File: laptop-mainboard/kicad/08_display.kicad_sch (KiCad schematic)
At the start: 8 parts, among them U36 TPD12S016, U37 SY6280_VLCD, U38 MP3389_Backlight

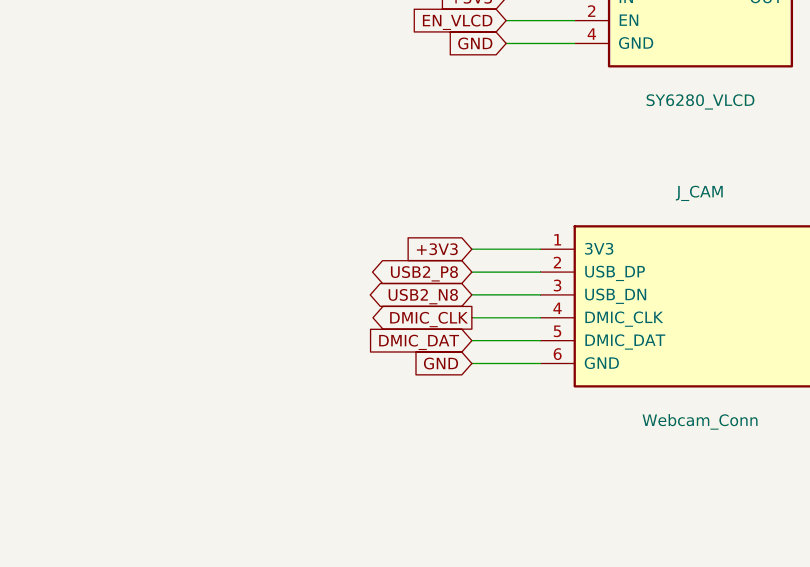
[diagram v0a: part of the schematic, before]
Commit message: Rev B: echte AM5-Pinbelegung, Kleinteile, EliteBook-850-G7-Format
- AM5-Pinmap (1718 Pins, WikiChip/Wikimedia Public Domain) als CSV,
  Sockel-Footprint mit echten Padnamen und 1708 Signal-Netzen im Board
- Blatt 10: MLCC-Baenke, 11 ESD-Arrays, USB2-Chokes, Straps; 48-MHz-Quarz;
  beidseitige Bestueckung (B.Cu) mit Kollisionspruefung pro Seite
- Board 340x112mm im EliteBook-850-G7-Layout: USB-C-100W-PD an der
  Barrel-Jack-Position, TB4/HDMI/USB-A/RJ45 rechts, USB-A/Klinke links,
  HP-Akku 3S/56Wh, HP-FPC-Steckplaetze (Pinouts zu verifizieren)
- GND-Stitching-Vias, MDI-/DP-Korridore, 645 Board-Netze
- Renderer tools/render_board.py erzeugt docs/board_render.png
- Doku: elitebook.md neu, grenzen.md/README/power/layout aktualisiert

Co-Authored-By: Claude Fable 5 <noreply@anthropic.com>
Claude-Session: https://claude.ai/code/session_01E8mU1RUAv938Hs69waADCc
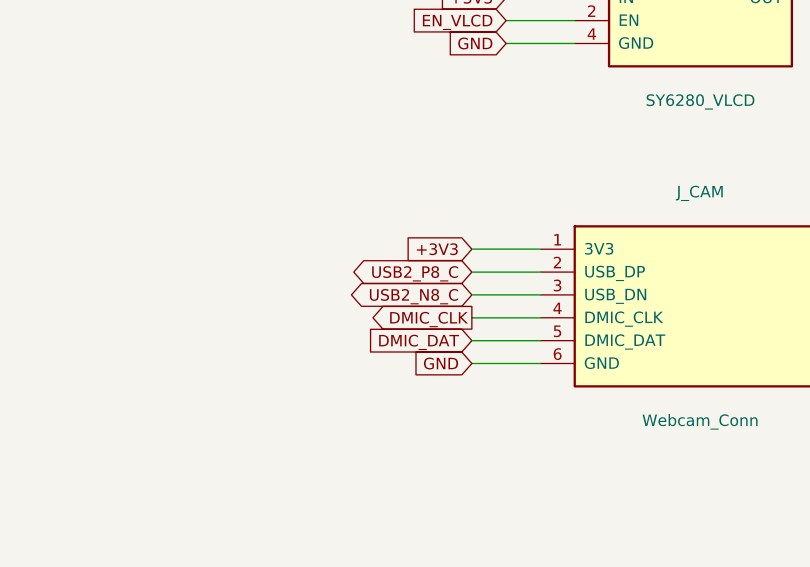
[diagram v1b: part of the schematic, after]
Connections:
- net USB2_N8 renamed USB2_N8_C
- net USB2_P8 renamed USB2_P8_C
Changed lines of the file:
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@@
     (pin "14")
     (pin "15")
-    (instances (project "laptop-mainboard" (path "/d22f2c28-8e23-5b8e-ba77-63ae2c13187c/9dd0bb70-e6d8-5534-8160-b27602d0556d" (reference "J_HDMI") (unit 1))))
+    (instances (project "laptop-mainboard" (path "/d22f2c28-8e23-5b8e-ba77-63ae2c13187c/bf71d2a7-0fa1-5bd7-a7a0-bc950c125fe0" (reference "J_HDMI") (unit 1))))
   )
   (wire (pts (xy 92.22 46.99) (xy 84.6 46.99)) (stroke (width 0) (type default)))
@@
     (pin "12")
     (pin "13")
-    (instances (project "laptop-mainboard" (path "/d22f2c28-8e23-5b8e-ba77-63ae2c13187c/9dd0bb70-e6d8-5534-8160-b27602d0556d" (reference "U36") (unit 1))))
+    (instances (project "laptop-mainboard" (path "/d22f2c28-8e23-5b8e-ba77-63ae2c13187c/bf71d2a7-0fa1-5bd7-a7a0-bc950c125fe0" (reference "U36") (unit 1))))
   )
   (wire (pts (xy 90.95 105.41) (xy 83.33 105.41)) (stroke (width 0) (type default)))
@@
     (pin "11")
     (pin "12")
-    (instances (project "laptop-mainboard" (path "/d22f2c28-8e23-5b8e-ba77-63ae2c13187c/9dd0bb70-e6d8-5534-8160-b27602d0556d" (reference "J_EDP") (unit 1))))
+    (instances (project "laptop-mainboard" (path "/d22f2c28-8e23-5b8e-ba77-63ae2c13187c/bf71d2a7-0fa1-5bd7-a7a0-bc950c125fe0" (reference "J_EDP") (unit 1))))
   )
   (wire (pts (xy 260.95 46.99) (xy 253.33 46.99)) (stroke (width 0) (type default)))
@@
     (pin "3")
     (pin "4")
-    (instances (project "laptop-mainboard" (path "/d22f2c28-8e23-5b8e-ba77-63ae2c13187c/9dd0bb70-e6d8-5534-8160-b27602d0556d" (reference "U37") (unit 1))))
+    (instances (project "laptop-mainboard" (path "/d22f2c28-8e23-5b8e-ba77-63ae2c13187c/bf71d2a7-0fa1-5bd7-a7a0-bc950c125fe0" (reference "U37") (unit 1))))
   )
   (wire (pts (xy 266.03 97.79) (xy 258.41 97.79)) (stroke (width 0) (type default)))
@@
     (pin "5")
     (pin "6")
-    (instances (project "laptop-mainboard" (path "/d22f2c28-8e23-5b8e-ba77-63ae2c13187c/9dd0bb70-e6d8-5534-8160-b27602d0556d" (reference "J_CAM") (unit 1))))
+    (instances (project "laptop-mainboard" (path "/d22f2c28-8e23-5b8e-ba77-63ae2c13187c/bf71d2a7-0fa1-5bd7-a7a0-bc950c125fe0" (reference "J_CAM") (unit 1))))
   )
   (wire (pts (xy 262.22 125.73) (xy 254.6 125.73)) (stroke (width 0) (type default)))
@@
   )
   (wire (pts (xy 262.22 128.27) (xy 254.6 128.27)) (stroke (width 0) (type default)))
-  (global_label "USB2_P8" (shape bidirectional) (at 254.6 128.27 180) (fields_autoplaced yes)
+  (global_label "USB2_P8_C" (shape bidirectional) (at 254.6 128.27 180) (fields_autoplaced yes)
     (effects (font (size 1.27 1.27)) (justify right))
     (property "Intersheetrefs" "${INTERSHEET_REFS}" (at 254.6 128.27 0) (effects (font (size 1.27 1.27)) (hide yes)))
   )
   (wire (pts (xy 262.22 130.81) (xy 254.6 130.81)) (stroke (width 0) (type default)))
-  (global_label "USB2_N8" (shape bidirectional) (at 254.6 130.81 180) (fields_autoplaced yes)
+  (global_label "USB2_N8_C" (shape bidirectional) (at 254.6 130.81 180) (fields_autoplaced yes)
     (effects (font (size 1.27 1.27)) (justify right))
     (property "Intersheetrefs" "${INTERSHEET_REFS}" (at 254.6 130.81 0) (effects (font (size 1.27 1.27)) (hide yes)))
@@
     (pin "6")
     (pin "7")
-    (instances (project "laptop-mainboard" (path "/d22f2c28-8e23-5b8e-ba77-63ae2c13187c/9dd0bb70-e6d8-5534-8160-b27602d0556d" (reference "U38") (unit 1))))
+    (instances (project "laptop-mainboard" (path "/d22f2c28-8e23-5b8e-ba77-63ae2c13187c/bf71d2a7-0fa1-5bd7-a7a0-bc950c125fe0" (reference "U38") (unit 1))))
   )
   (wire (pts (xy 443.49 46.99) (xy 435.87 46.99)) (stroke (width 0) (type default)))
@@
     (pin "1")
     (pin "2")
-    (instances (project "laptop-mainboard" (path "/d22f2c28-8e23-5b8e-ba77-63ae2c13187c/9dd0bb70-e6d8-5534-8160-b27602d0556d" (reference "L8") (unit 1))))
+    (instances (project "laptop-mainboard" (path "/d22f2c28-8e23-5b8e-ba77-63ae2c13187c/bf71d2a7-0fa1-5bd7-a7a0-bc950c125fe0" (reference "L8") (unit 1))))
   )
   (wire (pts (xy 448.57 77.47) (xy 440.95 77.47)) (stroke (width 0) (type default)))
@@
     (pin "1")
     (pin "2")
-    (instances (project "laptop-mainboard" (path "/d22f2c28-8e23-5b8e-ba77-63ae2c13187c/9dd0bb70-e6d8-5534-8160-b27602d0556d" (reference "D1") (unit 1))))
+    (instances (project "laptop-mainboard" (path "/d22f2c28-8e23-5b8e-ba77-63ae2c13187c/bf71d2a7-0fa1-5bd7-a7a0-bc950c125fe0" (reference "D1") (unit 1))))
   )
   (wire (pts (xy 448.57 100.33) (xy 440.95 100.33)) (stroke (width 0) (type default)))
